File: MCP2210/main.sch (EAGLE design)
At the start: 1 part, among them J1 USB_A_SMT_MALE

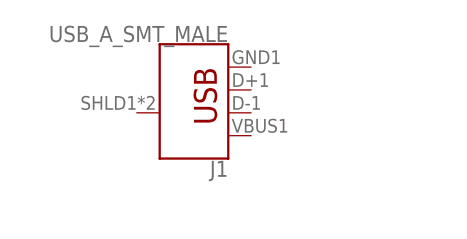
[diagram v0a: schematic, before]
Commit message: added crystal
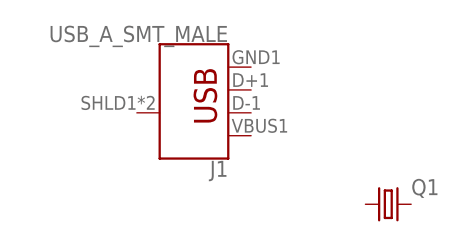
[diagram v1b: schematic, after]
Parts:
- added Q1: (no value), crystal:CRYSTALHC49U-V
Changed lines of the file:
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@@
 <parts>
 <part name="J1" library="SparkFun-Connectors" library_urn="urn:adsk.eagle:library:513" deviceset="USB_A" device="_SMT_MALE" package3d_urn="urn:adsk.eagle:package:38305/1"/>
+<part name="Q1" library="crystal" library_urn="urn:adsk.eagle:library:204" deviceset="CRYSTAL" device="HC49U-V" package3d_urn="urn:adsk.eagle:package:12075/1"/>
 </parts>
 <sheets>
@@
 <attribute name="VALUE" x="0" y="33.274" size="1.778" layer="96" font="vector" rot="R180" align="top-left"/>
 </instance>
+<instance part="Q1" gate="G$1" x="17.78" y="15.24">
+<attribute name="NAME" x="20.32" y="16.256" size="1.778" layer="95"/>
+<attribute name="VALUE" x="20.32" y="12.7" size="1.778" layer="96"/>
+</instance>
 </instances>
